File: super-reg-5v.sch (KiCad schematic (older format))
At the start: 36 parts, among them Q1 2SA1015, Q2 D44H11, U1 LM317T, U2 AD825, X1 AC_IN, X2 DC_OUT

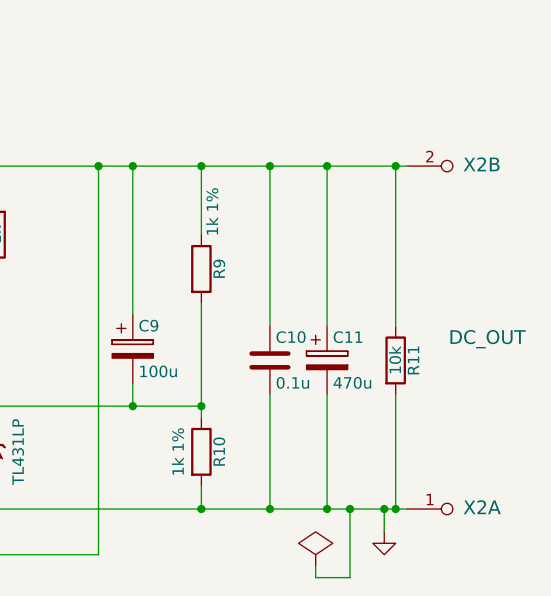
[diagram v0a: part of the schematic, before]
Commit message: change generic diode package to TUMD2 larger capacitor pad
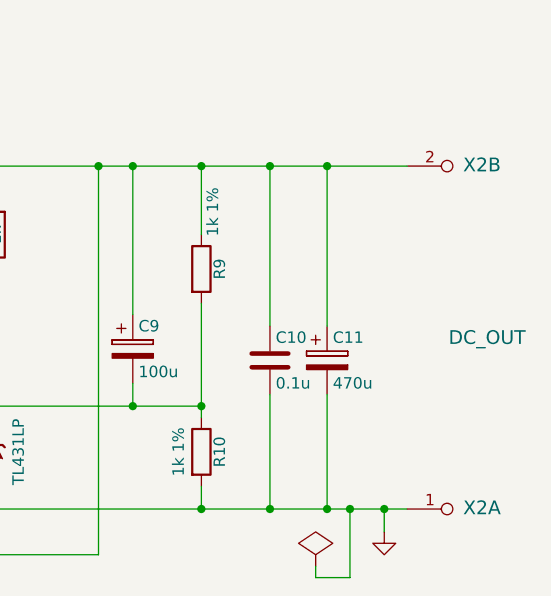
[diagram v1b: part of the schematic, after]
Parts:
- removed R11: 10k, Resistors_SMD:R_0603_HandSoldering, symbol R
- C1: footprint Capacitors_ThroughHole:C_Radial_D18_L36_P7.5 -> myfootprint:C_Radial_D18_L36_P7.5_LargePad
- D2, D4, D6: footprint Diodes_SMD:SMA_Handsoldering -> myfootprint:TUMD2-handsoldering
- JP1: footprint Connect:PINHEAD1-3 -> Pin_Headers:Pin_Header_Straight_1x03
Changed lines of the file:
@@
 LIBS:contrib
 LIBS:valves
+LIBS:references
+LIBS:ab2_terminal_block
+LIBS:DB-1
 LIBS:semi-trans-OnSemi
-LIBS:references
-LIBS:DB-1
-LIBS:ab2_terminal_block
 LIBS:super-reg-5v-cache
 EELAYER 25 0
@@
 F 0 "C1" H 2975 3550 50  0000 L CNN
 F 1 "2200u" H 2975 3350 50  0000 L CNN
-F 2 "Capacitors_ThroughHole:C_Radial_D18_L36_P7.5" H 2988 3300 50  0001 C CNN
+F 2 "myfootprint:C_Radial_D18_L36_P7.5_LargePad" H 2988 3300 50  0001 C CNN
 F 3 "" H 2950 3450 50  0000 C CNN
 	1    2950 3450
@@
 F 0 "JP1" H 6550 2350 50  0000 L CNN
 F 1 "OPAMP_PWR" H 6500 2550 50  0000 C BNN
-F 2 "Connect:PINHEAD1-3" H 6500 2450 50  0001 C CNN
+F 2 "Pin_Headers:Pin_Header_Straight_1x03" H 6500 2450 50  0001 C CNN
 F 3 "" H 6500 2450 50  0000 C CNN
 	1    6500 2450
@@
 F 0 "D6" H 7600 3700 50  0000 C CNN
 F 1 "D" H 7850 3600 50  0000 C CNN
-F 2 "Diodes_SMD:SMA_Handsoldering" H 7600 3600 50  0001 C CNN
+F 2 "myfootprint:TUMD2-handsoldering" H 7600 3600 50  0001 C CNN
 F 3 "" H 7600 3600 50  0000 C CNN
 	1    7600 3600
@@
 F 0 "D4" H 7400 3700 50  0000 C CNN
 F 1 "D" H 7150 3600 50  0000 C CNN
-F 2 "Diodes_SMD:SMA_Handsoldering" H 7400 3600 50  0001 C CNN
+F 2 "myfootprint:TUMD2-handsoldering" H 7400 3600 50  0001 C CNN
 F 3 "" H 7400 3600 50  0000 C CNN
 	1    7400 3600
@@
 F 0 "D2" H 3600 2450 50  0000 C CNN
 F 1 "D" H 3600 2250 50  0000 C CNN
-F 2 "Diodes_SMD:SMA_Handsoldering" H 3600 2350 50  0001 C CNN
+F 2 "myfootprint:TUMD2-handsoldering" H 3600 2350 50  0001 C CNN
 F 3 "" H 3600 2350 50  0000 C CNN
 	1    3600 2350
@@
 Wire Wire Line
 	3750 2350 4000 2350
-$Comp
-L R R11
-U 1 1 5794D9D1
-P 10150 3550
-F 0 "R11" V 10230 3550 50  0000 C CNN
-F 1 "10k" V 10150 3550 50  0000 C CNN
-F 2 "Resistors_SMD:R_0603_HandSoldering" V 10080 3550 50  0001 C CNN
-F 3 "" H 10150 3550 50  0000 C CNN
-	1    10150 3550
-	1    0    0    -1
-$EndComp
-Wire Wire Line
-	10150 3400 10150 2700
-Connection ~ 10150 2700
-Wire Wire Line
-	10150 3700 10150 4200
-Connection ~ 10150 4200
 $EndSCHEMATC

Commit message: larger via pad size change silk for bridge-diode D1
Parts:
- D1: footprint DB-1:D*** -> myfootprint:DB-1_DIP
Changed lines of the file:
@@
 F 0 "D1" H 2100 4100 60  0000 C CNN
 F 1 "DB-1S" V 2150 3450 60  0000 C CNN
-F 2 "DB-1:D***" H 2150 3450 60  0001 C CNN
+F 2 "myfootprint:DB-1_DIP" H 2150 3450 60  0001 C CNN
 F 3 "" H 2150 3450 60  0000 C CNN
 	1    2150 3450

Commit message: change recommended parts
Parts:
- C11: value 470u -> 220u OS-CON
- C3, C6: value 100u -> 100u 35v LowESR
- C5: value 100u -> 100u LowESR
- C8: value 100u -> 100u EP-Cap
- D3: value 2.7V -> ZD 2.7V
- LED1: value LED -> LED GREEN(2V)
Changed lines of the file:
@@
 P 4700 3050
 F 0 "LED1" H 4700 3150 50  0000 C CNN
-F 1 "LED" H 4700 2950 50  0000 C CNN
+F 1 "LED GREEN(2V)" H 4700 2950 50  0000 C CNN
 F 2 "LEDs:LED-5MM" H 4700 3050 50  0001 C CNN
 F 3 "" H 4700 3050 50  0000 C CNN
@@
 P 5800 3600
 F 0 "D3" H 5800 3700 50  0000 C CNN
-F 1 "2.7V" H 5800 3500 50  0000 C CNN
+F 1 "ZD 2.7V" H 5800 3500 50  0000 C CNN
 F 2 "Diodes_ThroughHole:Diode_DO-35_SOD27_Horizontal_RM10" H 5800 3600 50  0001 C CNN
 F 3 "" H 5800 3600 50  0000 C CNN
@@
 P 4250 3450
 F 0 "C3" H 4275 3550 50  0000 L CNN
-F 1 "100u" H 4275 3350 50  0000 L CNN
+F 1 "100u 35v LowESR" H 4250 3650 50  0000 L CNN
 F 2 "Capacitors_ThroughHole:C_Radial_D6.3_L11.2_P2.5" H 4288 3300 50  0001 C CNN
 F 3 "" H 4250 3450 50  0000 C CNN
@@
 P 6100 2300
 F 0 "C6" H 6125 2400 50  0000 L CNN
-F 1 "100u" H 6125 2200 50  0000 L CNN
+F 1 "100u 35v LowESR" H 5350 2450 50  0000 L CNN
 F 2 "Capacitors_ThroughHole:C_Radial_D6.3_L11.2_P2.5" H 6138 2150 50  0001 C CNN
 F 3 "" H 6100 2300 50  0000 C CNN
@@
 P 5800 3900
 F 0 "C5" H 5825 4000 50  0000 L CNN
-F 1 "100u" H 5825 3800 50  0000 L CNN
+F 1 "100u LowESR" V 5650 3650 50  0000 L CNN
 F 2 "Capacitors_ThroughHole:C_Radial_D6.3_L11.2_P2.5" H 5838 3750 50  0001 C CNN
 F 3 "" H 5800 3900 50  0000 C CNN
@@
 P 7850 3950
 F 0 "C8" H 7875 4050 50  0000 L CNN
-F 1 "100u" H 7875 3850 50  0000 L CNN
+F 1 "100u EP-Cap" H 7500 3800 50  0000 L CNN
 F 2 "Capacitors_ThroughHole:C_Radial_D8_L13_P3.8" H 7888 3800 50  0001 C CNN
 F 3 "" H 7850 3950 50  0000 C CNN
@@
 P 9850 3550
 F 0 "C11" H 9875 3650 50  0000 L CNN
-F 1 "470u" H 9875 3450 50  0000 L CNN
+F 1 "220u OS-CON" H 9875 3450 50  0000 L CNN
 F 2 "Capacitors_ThroughHole:C_Radial_D10_L20_P5" H 9888 3400 50  0001 C CNN
 F 3 "" H 9850 3550 50  0000 C CNN

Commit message: change footprint for the diode add an alternate op-amp footprint
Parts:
- added U3: AD825, Housings_SOIC:SOIC-8_3.9x4.9mm_Pitch1.27mm, symbol TL081
- D2: footprint myfootprint:TUMD2-handsoldering -> Diodes_SMD:SMA_Handsoldering
- D4, D6: footprint myfootprint:TUMD2-handsoldering -> myfootprint:UMD2-handsoldering
- R8: value 1k -> 2.2k
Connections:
- net GND: now also U3.4 (V-)
- net at R6.1, U2.6: now also U3.6
- net OPAMP_N: now reaches C9.2, D4.1 (K), D6.2 (A), R10.1, R9.2, U2.2 (-)
- net OPAMP_N: now also U3.2 (-)
- net OPAMP_P: now reaches C8.1, D4.2 (A), D6.1 (K), R7.2, U2.3 (+)
- net OPAMP_P: now also U3.3 (+)
- net OPAMP_PW: now reaches C7.1, JP1.2, U2.7 (V+)
- net OPAMP_PW: now also U3.7 (V+)
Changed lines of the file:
@@
 F 0 "D6" H 7600 3700 50  0000 C CNN
 F 1 "D" H 7850 3600 50  0000 C CNN
-F 2 "myfootprint:TUMD2-handsoldering" H 7600 3600 50  0001 C CNN
+F 2 "myfootprint:UMD2-handsoldering" H 7600 3600 50  0001 C CNN
 F 3 "" H 7600 3600 50  0000 C CNN
 	1    7600 3600
@@
 F 0 "D4" H 7400 3700 50  0000 C CNN
 F 1 "D" H 7150 3600 50  0000 C CNN
-F 2 "myfootprint:TUMD2-handsoldering" H 7400 3600 50  0001 C CNN
+F 2 "myfootprint:UMD2-handsoldering" H 7400 3600 50  0001 C CNN
 F 3 "" H 7400 3600 50  0000 C CNN
 	1    7400 3600
@@
 P 8400 3000
 F 0 "R8" V 8480 3000 50  0000 C CNN
-F 1 "1k" V 8400 3000 50  0000 C CNN
+F 1 "2.2k" V 8400 3000 50  0000 C CNN
 F 2 "Resistors_SMD:R_0603_HandSoldering" V 8330 3000 50  0001 C CNN
 F 3 "" H 8400 3000 50  0000 C CNN
@@
 F 0 "D2" H 3600 2450 50  0000 C CNN
 F 1 "D" H 3600 2250 50  0000 C CNN
-F 2 "myfootprint:TUMD2-handsoldering" H 3600 2350 50  0001 C CNN
+F 2 "Diodes_SMD:SMA_Handsoldering" H 3600 2350 50  0001 C CNN
 F 3 "" H 3600 2350 50  0000 C CNN
 	1    3600 2350
@@
 Wire Wire Line
 	3750 2350 4000 2350
+$Comp
+L TL081 U3
+U 1 1 57C2A197
+P 6900 4900
+F 0 "U3" H 6900 5150 50  0000 L CNN
+F 1 "AD825" H 6900 5050 50  0000 L CNN
+F 2 "Housings_SOIC:SOIC-8_3.9x4.9mm_Pitch1.27mm" H 6950 5100 50  0001 C CNN
+F 3 "" H 6900 5150 50  0000 C CNN
+	1    6900 4900
+	-1   0    0    -1
+$EndComp
+Wire Wire Line
+	7000 5200 7000 5350
+Wire Wire Line
+	6600 4900 6400 4900
+Wire Wire Line
+	6400 4900 6400 3600
+Connection ~ 6400 3600
+$Comp
+L GND #PWR06
+U 1 1 57C2A3B3
+P 7000 5350
+F 0 "#PWR06" H 7000 5350 30  0001 C CNN
+F 1 "GND" H 7000 5280 30  0001 C CNN
+F 2 "" H 7000 5350 60  0000 C CNN
+F 3 "" H 7000 5350 60  0000 C CNN
+	1    7000 5350
+	1    0    0    -1
+$EndComp
+Text Label 7000 3000 0    60   ~ 0
+OPAMP_PW
+Text Label 7000 4600 0    60   ~ 0
+OPAMP_PW
+Text Label 7200 4800 0    60   ~ 0
+OPAMP_P
+Text Label 7400 3450 0    60   ~ 0
+OPAMP_P
+Text Label 7200 5000 0    60   ~ 0
+OPAMP_N
+Text Label 7600 3750 0    60   ~ 0
+OPAMP_N
 $EndSCHEMATC

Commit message: change PCB size (35mm x 85mm) add alternate C1
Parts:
- added C12: C1-Alt, myfootprint:C_Radial_D18_L36_P7.5_LargePad_NoCircle, symbol CP
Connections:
- net GND: now also C12.2
- net at C1.1, C2.1, D1.3 (+)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: now also C12.1
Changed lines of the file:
@@
 Text Label 7600 3750 0    60   ~ 0
 OPAMP_N
+$Comp
+L CP C12
+U 1 1 57EA6AB0
+P 2750 3750
+F 0 "C12" H 2775 3850 50  0000 L CNN
+F 1 "C1-Alt" H 2775 3650 50  0000 L CNN
+F 2 "myfootprint:C_Radial_D18_L36_P7.5_LargePad_NoCircle" H 2788 3600 50  0001 C CNN
+F 3 "" H 2750 3750 50  0000 C CNN
+	1    2750 3750
+	1    0    0    -1
+$EndComp
+Wire Wire Line
+	2750 3600 2750 2700
+Connection ~ 2750 2700
+Wire Wire Line
+	2750 3900 2750 4200
+Connection ~ 2750 4200
 $EndSCHEMATC

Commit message: add alternate bridge diode
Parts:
- added D7: AlterBridgeD, w_pth_diodes:bridge_wob_alter_pin, symbol Diode_Bridge
- C11: footprint Capacitors_ThroughHole:C_Radial_D10_L20_P5 -> Capacitors_ThroughHole:C_Radial_D8_L13_P3.8
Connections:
- net GND: now also D7.1 (-)
- net at C1.1, C12.1, C2.1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: now also D7.3 (+)
- net at D1.1 (AC), X1.1: now also D7.2
- net at D1.2 (AC), X1.2: now also D7.4
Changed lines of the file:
@@
 F 0 "C11" H 9875 3650 50  0000 L CNN
 F 1 "220u OS-CON" H 9875 3450 50  0000 L CNN
-F 2 "Capacitors_ThroughHole:C_Radial_D10_L20_P5" H 9888 3400 50  0001 C CNN
+F 2 "Capacitors_ThroughHole:C_Radial_D8_L13_P3.8" H 9888 3400 50  0001 C CNN
 F 3 "" H 9850 3550 50  0000 C CNN
 	1    9850 3550
@@
 	2550 3450 2650 3450
 Wire Wire Line
-	2650 3450 2650 2700
+	2650 2700 2650 4850
 Connection ~ 2950 2700
 Wire Wire Line
 	2150 3050 2150 3000
 Wire Wire Line
-	2150 3000 1400 3000
+	1400 3000 2300 3000
 Wire Wire Line
 	9800 4450 9800 4500
@@
 $EndComp
 Wire Wire Line
-	1500 3900 1500 4000
+	1500 3900 1500 5250
 Connection ~ 1500 4000
 Wire Wire Line
@@
 	2750 3900 2750 4200
 Connection ~ 2750 4200
+$Comp
+L Diode_Bridge D7
+U 1 1 57EBD8BE
+P 2150 4850
+F 0 "D7" H 1900 5150 50  0000 C CNN
+F 1 "AlterBridgeD" H 2500 4500 50  0000 C CNN
+F 2 "w_pth_diodes:bridge_wob_alter_pin" H 2150 4850 50  0001 C CNN
+F 3 "" H 2150 4850 50  0000 C CNN
+	1    2150 4850
+	1    0    0    -1
+$EndComp
+Wire Wire Line
+	2150 4450 2150 4400
+Wire Wire Line
+	2150 4400 2300 4400
+Wire Wire Line
+	2300 4400 2300 3000
+Connection ~ 2150 3000
+Wire Wire Line
+	1500 5250 2150 5250
+Wire Wire Line
+	1750 4850 1750 4200
+Connection ~ 1750 4200
+Wire Wire Line
+	2650 4850 2550 4850
+Connection ~ 2650 3450
 $EndSCHEMATC

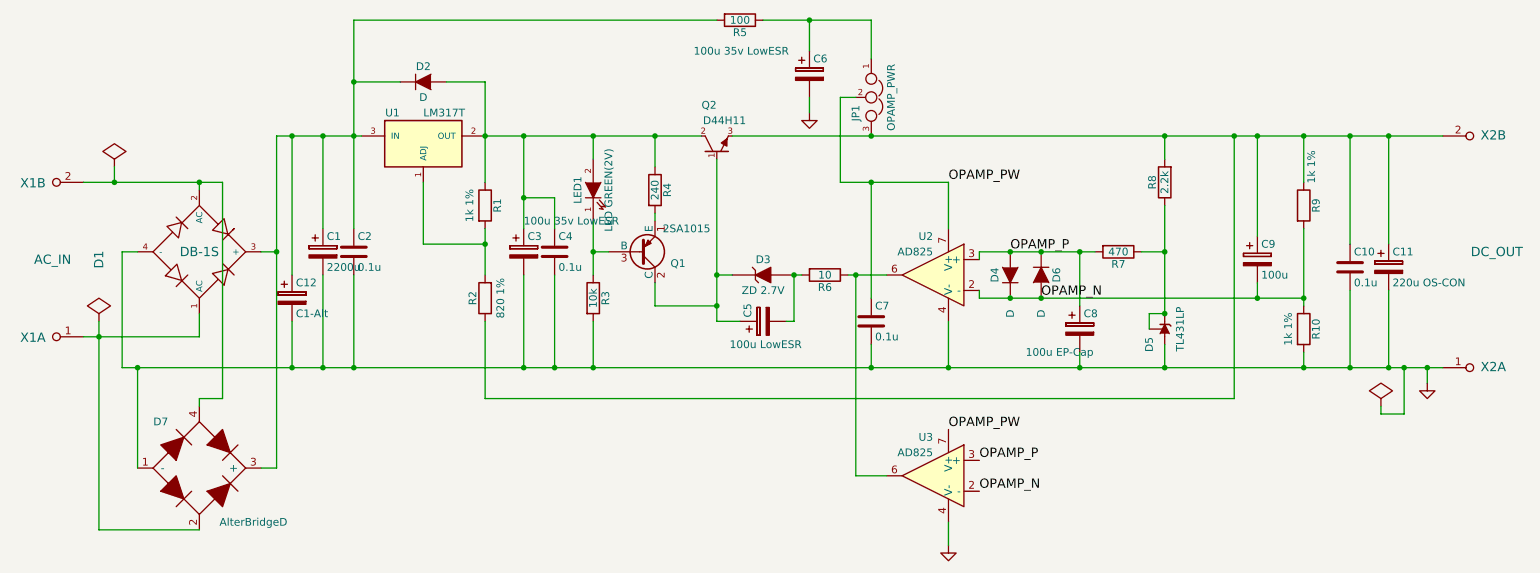
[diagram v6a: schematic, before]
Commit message: change the alternate bridge-D to single bridge diodes
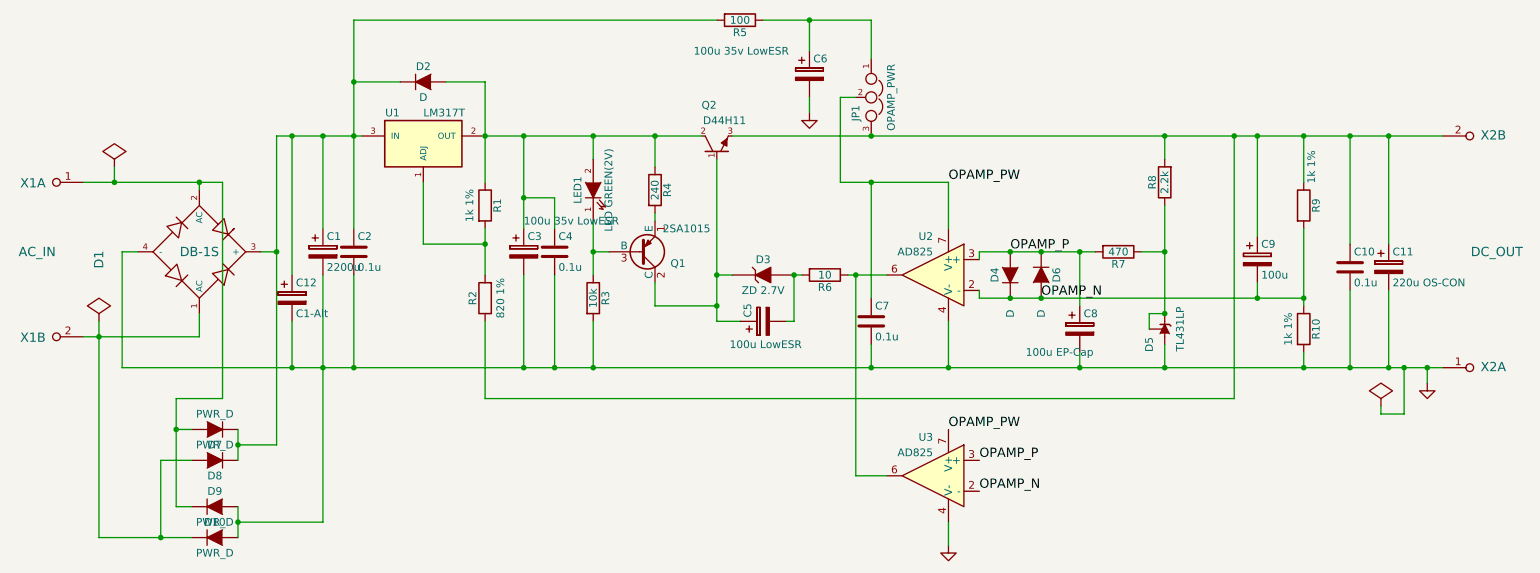
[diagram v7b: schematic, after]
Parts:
- removed D7: AlterBridgeD, w_pth_diodes:bridge_wob_alter_pin, symbol Diode_Bridge
- added D10, D7, D8, D9: PWR_D, Diodes_ThroughHole:Diode_DO-41_SOD81_Horizontal_RM10, symbol D
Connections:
- net GND: now also D10.2 (A), D9.2 (A)
- net at C1.1, C12.1, C2.1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: now also D7.1 (K), D8.1 (K)
- net at D1.1 (AC): now also X1.2, D10.1 (K), D8.2 (A); no longer X1.1
- net at D1.2 (AC): now also X1.1, D7.2 (A), D9.1 (K); no longer X1.2
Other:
- moved on the sheet: X1A, X1B
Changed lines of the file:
@@
 	6000 3600 6050 3600
 Wire Wire Line
-	6600 3600 6350 3600
+	6350 3600 6600 3600
 Wire Wire Line
 	4700 2700 4700 2850
@@
 Connection ~ 3150 2700
 Wire Wire Line
-	2950 3600 2950 4200
+	2950 3600 2950 5200
 Connection ~ 4250 4200
 Wire Wire Line
@@
 Connection ~ 9850 4200
 Wire Wire Line
-	2150 3850 2150 4000
-Wire Wire Line
-	2150 4000 1400 4000
+	2150 4000 2150 3850
+Wire Wire Line
+	1400 4000 2150 4000
 Wire Wire Line
 	1750 3450 1650 3450
@@
 	2550 3450 2650 3450
 Wire Wire Line
-	2650 2700 2650 4850
+	2650 2700 2650 4700
 Connection ~ 2950 2700
 Wire Wire Line
-	2150 3050 2150 3000
+	2150 3000 2150 3050
 Wire Wire Line
 	1400 3000 2300 3000
@@
 L AB2_AKZ500_02 X1
 U 1 1 5794C231
+P 1400 3000
+F 0 "X1" H 1155 2995 60  0000 R CNN
+F 1 "AC_IN" H 1300 3200 60  0001 C CNN
+F 2 "Terminal_Blocks:TerminalBlock_Pheonix_MKDS1.5-2pol" H 1400 3000 60  0001 C CNN
+F 3 "" H 1400 3000 60  0000 C CNN
+	1    1400 3000
+	1    0    0    -1
+$EndComp
+$Comp
+L AB2_AKZ500_02 X1
+U 2 1 5794C29D
 P 1400 4000
 F 0 "X1" H 1155 3995 60  0000 R CNN
-F 1 "AC_IN" H 1300 4200 60  0001 C CNN
+F 1 "AC_IN" H 1100 4550 60  0000 C CNN
 F 2 "Terminal_Blocks:TerminalBlock_Pheonix_MKDS1.5-2pol" H 1400 4000 60  0001 C CNN
 F 3 "" H 1400 4000 60  0000 C CNN
-	1    1400 4000
-	1    0    0    -1
-$EndComp
-$Comp
-L AB2_AKZ500_02 X1
-U 2 1 5794C29D
-P 1400 3000
-F 0 "X1" H 1155 2995 60  0000 R CNN
-F 1 "AC_IN" H 1200 2500 60  0000 C CNN
-F 2 "Terminal_Blocks:TerminalBlock_Pheonix_MKDS1.5-2pol" H 1400 3000 60  0001 C CNN
-F 3 "" H 1400 3000 60  0000 C CNN
-	2    1400 3000
+	2    1400 4000
 	1    0    0    -1
 $EndComp
@@
 $EndComp
 Wire Wire Line
-	1500 3900 1500 5250
+	1500 3900 1500 5300
 Connection ~ 1500 4000
 Wire Wire Line
@@
 	2750 3900 2750 4200
 Connection ~ 2750 4200
-$Comp
-L Diode_Bridge D7
-U 1 1 57EBD8BE
-P 2150 4850
-F 0 "D7" H 1900 5150 50  0000 C CNN
-F 1 "AlterBridgeD" H 2500 4500 50  0000 C CNN
-F 2 "w_pth_diodes:bridge_wob_alter_pin" H 2150 4850 50  0001 C CNN
-F 3 "" H 2150 4850 50  0000 C CNN
-	1    2150 4850
-	1    0    0    -1
-$EndComp
-Wire Wire Line
-	2150 4450 2150 4400
-Wire Wire Line
-	2150 4400 2300 4400
-Wire Wire Line
-	2300 4400 2300 3000
+Wire Wire Line
+	2300 3000 2300 4400
 Connection ~ 2150 3000
-Wire Wire Line
-	1500 5250 2150 5250
-Wire Wire Line
-	1750 4850 1750 4200
-Connection ~ 1750 4200
-Wire Wire Line
-	2650 4850 2550 4850
 Connection ~ 2650 3450
+$Comp
+L D D7
+U 1 1 5803BCE0
+P 2250 4600
+F 0 "D7" H 2250 4700 50  0000 C CNN
+F 1 "PWR_D" H 2250 4500 50  0000 C CNN
+F 2 "Diodes_ThroughHole:Diode_DO-41_SOD81_Horizontal_RM10" H 2250 4600 50  0001 C CNN
+F 3 "" H 2250 4600 50  0000 C CNN
+	1    2250 4600
+	-1   0    0    1
+$EndComp
+$Comp
+L D D8
+U 1 1 5803BD92
+P 2250 4800
+F 0 "D8" H 2250 4900 50  0000 C CNN
+F 1 "PWR_D" H 2250 4700 50  0000 C CNN
+F 2 "Diodes_ThroughHole:Diode_DO-41_SOD81_Horizontal_RM10" H 2250 4800 50  0001 C CNN
+F 3 "" H 2250 4800 50  0000 C CNN
+	1    2250 4800
+	-1   0    0    1
+$EndComp
+$Comp
+L D D9
+U 1 1 5803BE26
+P 2250 5100
+F 0 "D9" H 2250 5200 50  0000 C CNN
+F 1 "PWR_D" H 2250 5000 50  0000 C CNN
+F 2 "Diodes_ThroughHole:Diode_DO-41_SOD81_Horizontal_RM10" H 2250 5100 50  0001 C CNN
+F 3 "" H 2250 5100 50  0000 C CNN
+	1    2250 5100
+	1    0    0    -1
+$EndComp
+$Comp
+L D D10
+U 1 1 5803BEB4
+P 2250 5300
+F 0 "D10" H 2250 5400 50  0000 C CNN
+F 1 "PWR_D" H 2250 5200 50  0000 C CNN
+F 2 "Diodes_ThroughHole:Diode_DO-41_SOD81_Horizontal_RM10" H 2250 5300 50  0001 C CNN
+F 3 "" H 2250 5300 50  0000 C CNN
+	1    2250 5300
+	1    0    0    -1
+$EndComp
+Wire Wire Line
+	2400 4600 2400 4800
+Wire Wire Line
+	2650 4700 2400 4700
+Connection ~ 2400 4700
+Wire Wire Line
+	2100 4600 2000 4600
+Wire Wire Line
+	2000 4400 2000 5100
+Wire Wire Line
+	2000 5100 2100 5100
+Wire Wire Line
+	2100 4800 1900 4800
+Wire Wire Line
+	1900 4800 1900 5300
+Wire Wire Line
+	1500 5300 2100 5300
+Connection ~ 1900 5300
+Wire Wire Line
+	2300 4400 2000 4400
+Connection ~ 2000 4600
+Wire Wire Line
+	2400 5100 2400 5300
+Wire Wire Line
+	2950 5200 2400 5200
+Connection ~ 2400 5200
 $EndSCHEMATC
